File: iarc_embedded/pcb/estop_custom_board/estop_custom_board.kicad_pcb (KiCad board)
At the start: 2 copper layers, 5 parts, among them J1 RECEIVER, Q1 IRF8301M, Q2 IRF8301M, Q3 IRF8301M, U1 LM341T-05_TO220

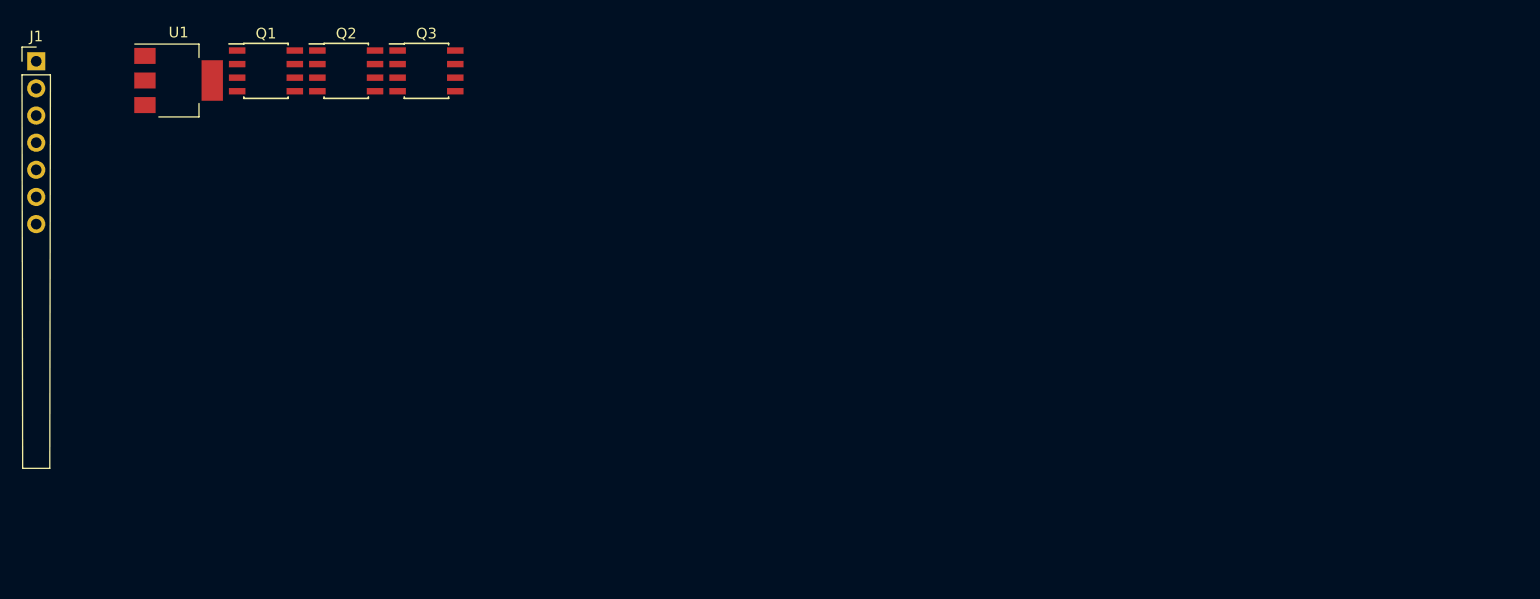
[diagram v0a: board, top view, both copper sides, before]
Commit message: NodeMCU ESP8266 embedded
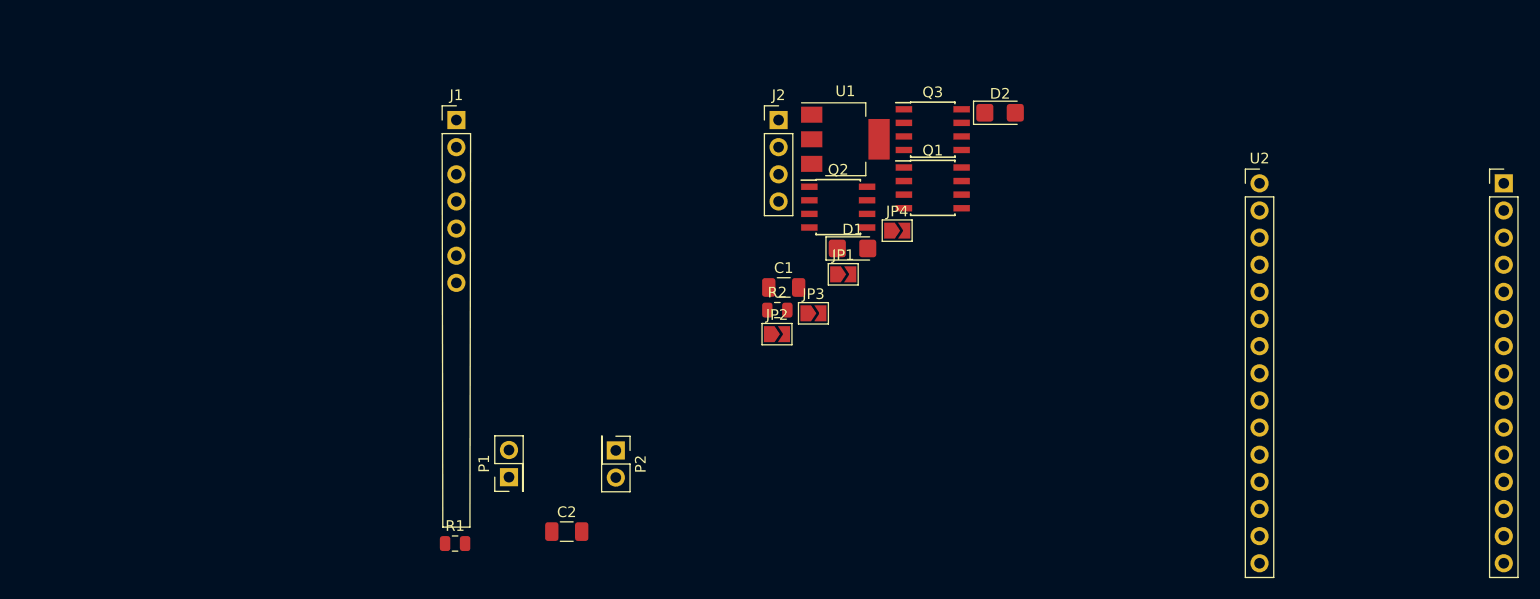
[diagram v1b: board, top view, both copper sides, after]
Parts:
- added C1: 4.7uF, Capacitor_SMD:C_1206_3216Metric, F.Cu at (198.7, 103.2)
- added C2: 10uF, Capacitor_SMD:C_1206_3216Metric, F.Cu at (178.4, 126.1)
- added D1: LED_GREEN, LED_SMD:LED_1206_3216Metric_Castellated, F.Cu at (205.2, 99.6)
- added D2: LED_RED, LED_SMD:LED_1206_3216Metric_Castellated, F.Cu at (219.0, 86.9)
- added J2: Conn_01x04, Connector_PinHeader_2.54mm:PinHeader_1x04_P2.54mm_Vertical, F.Cu at (198.2, 87.6)
- added JP1: Jumper, Jumper:SolderJumper-2_P1.3mm_Open_TrianglePad1.0x1.5mm, F.Cu at (204.3, 102.0)
- added JP2: Jumper, Jumper:SolderJumper-2_P1.3mm_Open_TrianglePad1.0x1.5mm, F.Cu at (198.1, 107.6)
- added JP3: Jumper, Jumper:SolderJumper-2_P1.3mm_Open_TrianglePad1.0x1.5mm, F.Cu at (201.5, 105.7)
- added JP4: Jumper, Jumper:SolderJumper-2_P1.3mm_Open_TrianglePad1.0x1.5mm, F.Cu at (209.3, 97.9)
- added P1: HEADER2, Connector_PinHeader_2.54mm:PinHeader_2x01_P2.54mm_Vertical, F.Cu at (173.0, 121.0)
- added P2: TOMOTORS, Connector_PinHeader_2.54mm:PinHeader_2x01_P2.54mm_Vertical, F.Cu at (183.0, 118.5)
- added R1: 475, Resistor_SMD:R_0805_2012Metric, F.Cu at (168.0, 127.2)
- added R2: 475, Resistor_SMD:R_0805_2012Metric, F.Cu at (198.1, 105.4)
- added U2: ESP8266-nodemcu, roomba_pcb:NODEMCU, F.Cu at (243.2, 93.5)
- moved Q1 63.4 mm to (212.7, 93.9)
- moved U1 62.7 mm to (204.5, 89.4)
- moved Q2 47.8 mm to (203.8, 95.7)
- moved Q3 47.7 mm to (212.7, 88.5)
- moved J1 39.7 mm to (168.1, 87.6)
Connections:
- J1 pad 3: (no net) -> Net-(J1-Pad3)
- J1 pad 4: (no net) -> Net-(J1-Pad4)
- J1 pad 5: (no net) -> Net-(J1-Pad5)
- J1 pad 6: (no net) -> Net-(J1-Pad6)
- U1 pad 1: (no net) -> +BATT

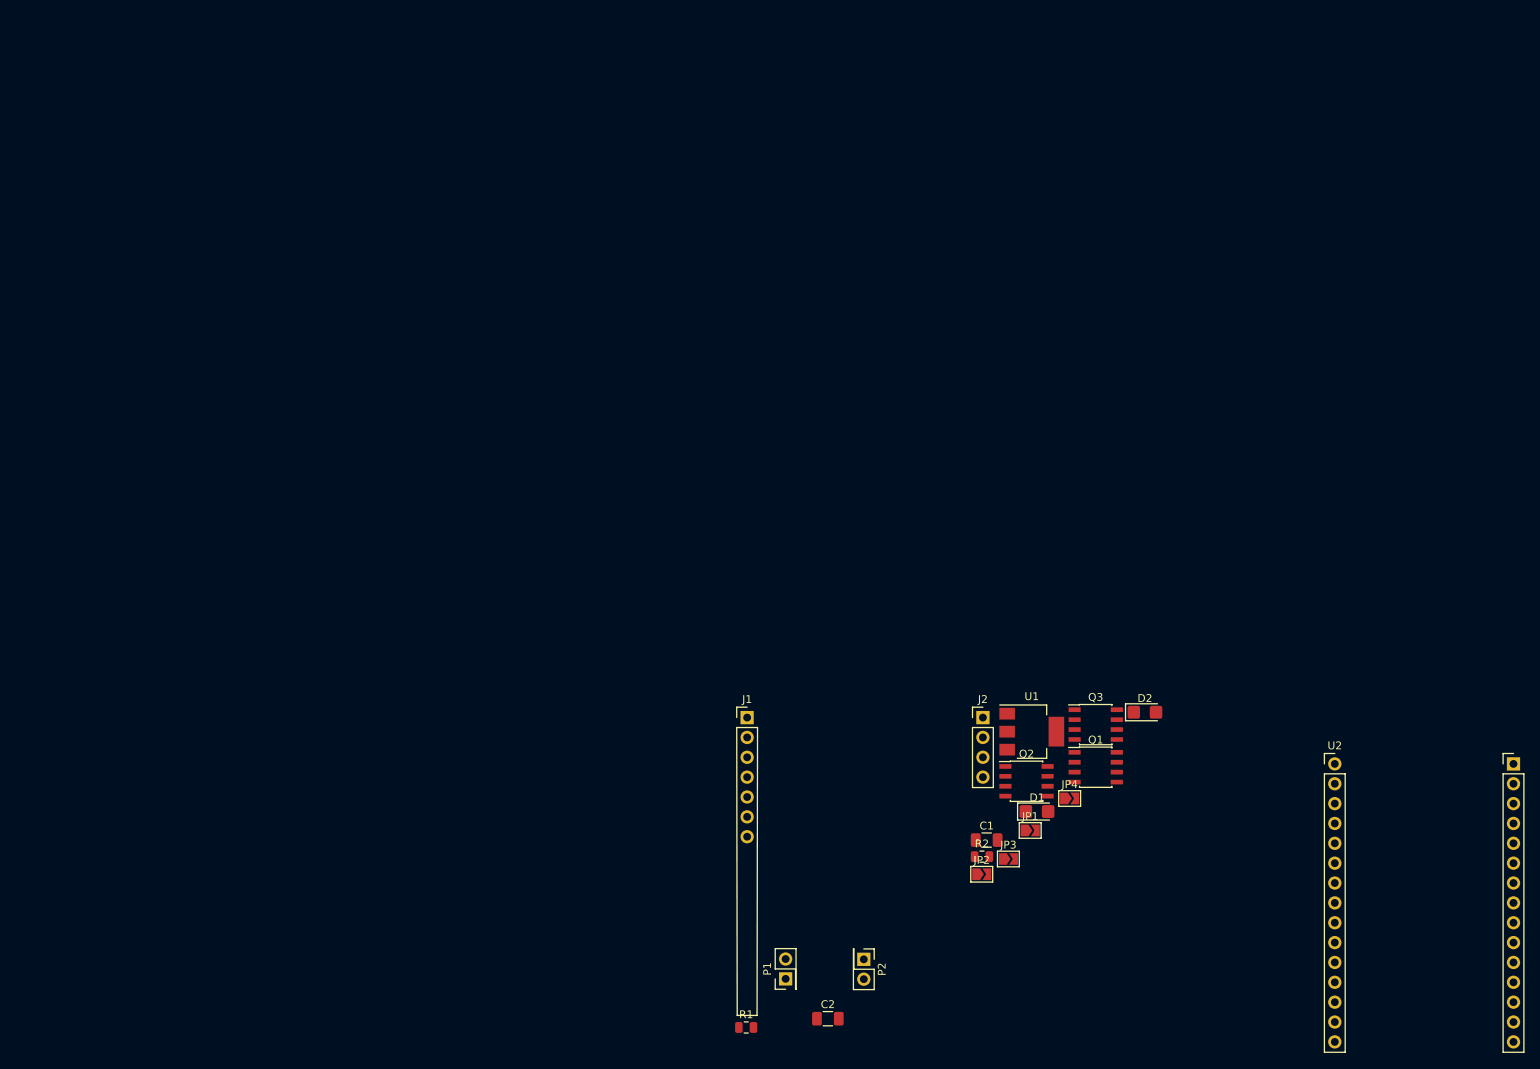
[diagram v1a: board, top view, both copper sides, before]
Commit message: PCB is laid out
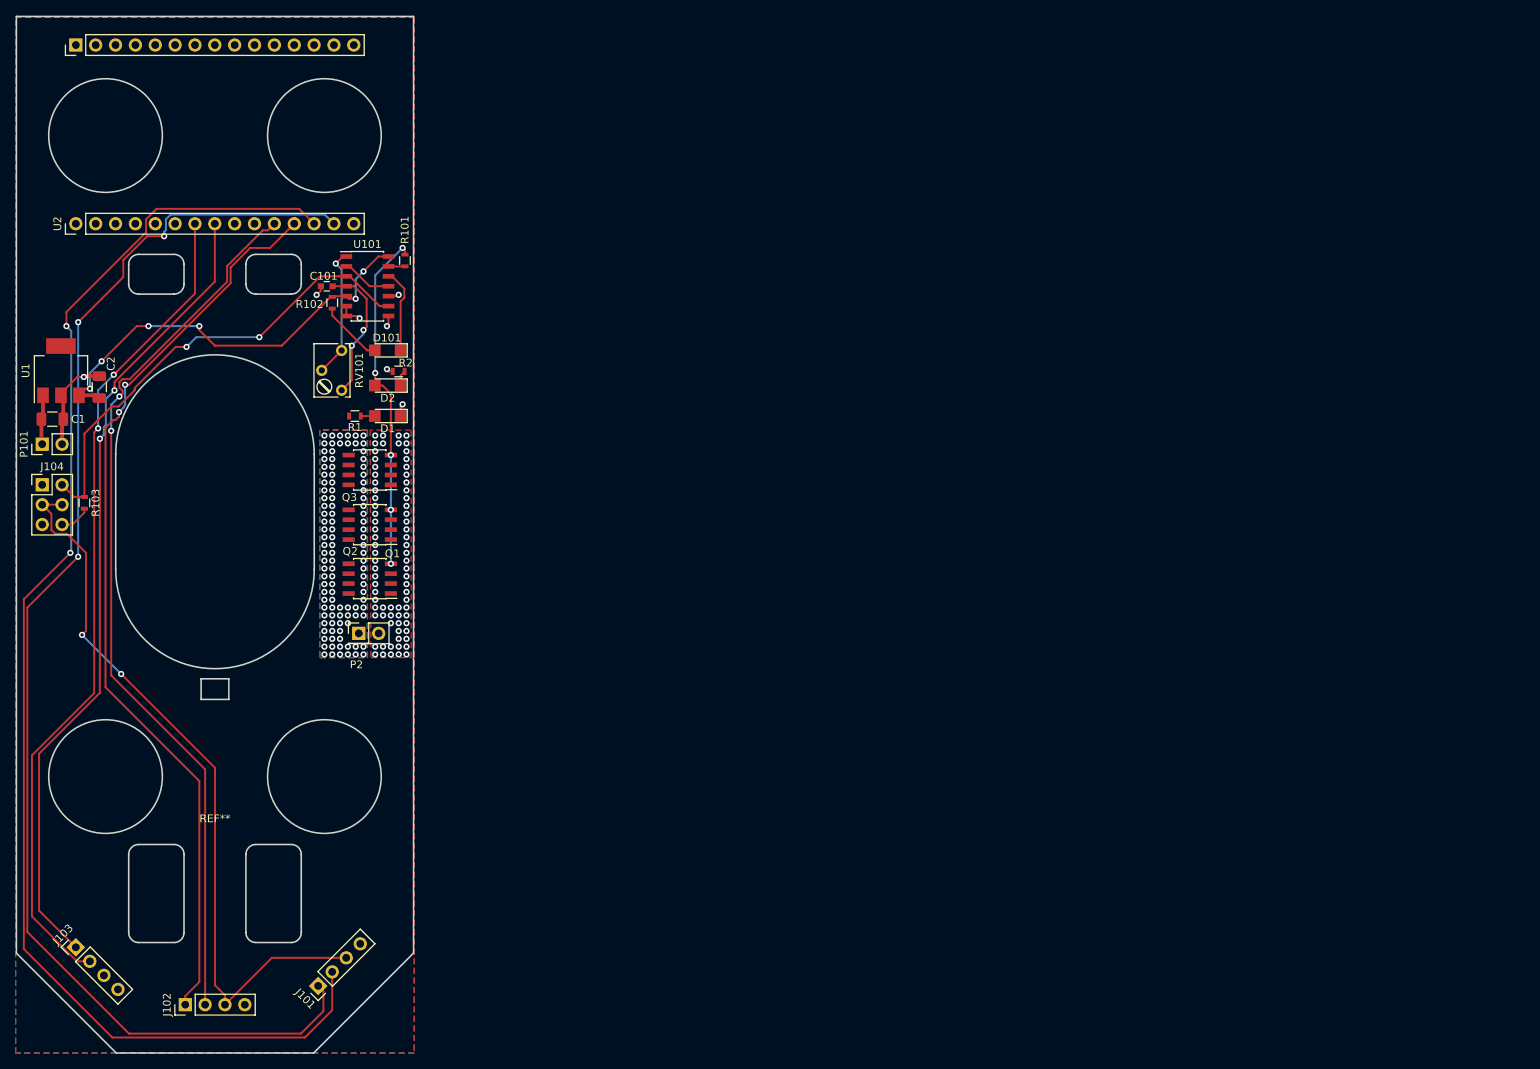
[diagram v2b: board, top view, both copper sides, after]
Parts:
- removed J1: RECEIVER, roomba_pcb:Receiver_IARC
- removed J2: Conn_01x04, Connector_PinHeader_2.54mm:PinHeader_1x04_P2.54mm_Vertical
- removed JP1, JP2, JP3, JP4: Jumper, Jumper:SolderJumper-2_P1.3mm_Open_TrianglePad1.0x1.5mm
- removed P1: HEADER2, Connector_PinHeader_2.54mm:PinHeader_2x01_P2.54mm_Vertical
- added C101: 1uF, Capacitors_SMD:C_0603, F.Cu at (114.3, 32.4)
- added D101: LED_RED, LEDs:LED_1206, F.Cu at (122.1, 40.6)
- added J101: Conn_01x04, Pin_Headers:Pin_Header_Straight_1x04_Pitch2.54mm, F.Cu at (113.2, 121.9)
- added J102: Conn_01x04, Pin_Headers:Pin_Header_Straight_1x04_Pitch2.54mm, F.Cu at (96.2, 124.3)
- added J103: Conn_01x04, Pin_Headers:Pin_Header_Straight_1x04_Pitch2.54mm, F.Cu at (82.2, 117.0)
- added J104: Conn_02x03_Odd_Even, Pin_Headers:Pin_Header_Straight_2x03_Pitch2.54mm, F.Cu at (77.9, 57.8)
- added P101: BATT, Pin_Headers:Pin_Header_Straight_1x02_Pitch2.54mm, F.Cu at (77.9, 52.6)
- added R101: 10, Resistors_SMD:R_0603, F.Cu at (124.3, 29.1)
- added R102: 475, Resistors_SMD:R_0603, F.Cu at (115.0, 34.5)
- added R103: 10k, Resistors_SMD:R_0603, F.Cu at (83.3, 60.1)
- added REF**: Outline, roomba_pcb:Outline, F.Cu at (100.0, 100.0)
- added RV101: 5k, Potentiometers:Potentiometer_Trimmer_Bourns_3266W, F.Cu at (116.2, 45.7)
- added U101: CD4013BM, Housings_SOIC:SOIC-14_3.9x8.7mm_Pitch1.27mm, F.Cu at (119.5, 32.4)
- D1, D2: footprint LED_SMD:LED_1206_3216Metric_Castellated -> LEDs:LED_1206
- P2: value TOMOTORS -> GND_INTERUPT
- R1, R2: footprint Resistor_SMD:R_0805_2012Metric -> Resistors_SMD:R_0603
- moved U2 175.2 mm to (82.2, 24.4), turned to 90 degrees
- moved U1 132.5 mm to (80.3, 43.2), turned to 90 degrees
- moved C1 131.1 mm to (79.2, 49.4)
- moved C2 123.3 mm to (85.2, 45.3), turned to 90 degrees
- moved D2 105.5 mm to (122.1, 45.1), turned to 180 degrees
- moved Q3 98.4 mm to (119.8, 55.9), turned to 180 degrees
- moved D1 97.3 mm to (122.1, 49.0), turned to 180 degrees
- moved R2 97.1 mm to (123.5, 43.3), turned to 180 degrees
- moved Q1 95.9 mm to (119.8, 69.8), turned to 180 degrees
- moved R1 92.9 mm to (117.9, 49.0), turned to 180 degrees
- moved Q2 90.2 mm to (119.8, 62.9), turned to 180 degrees
- moved P2 76.9 mm to (118.4, 76.8), turned to 0 degrees
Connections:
- P2 pad 1: +BATT -> Net-(P2-Pad1)
- P2 pad 2: Net-(P2-Pad2) -> GND
- Q1 pad 5: Net-(P2-Pad2) -> Net-(P2-Pad1)
- Q1 pad 6: Net-(P2-Pad2) -> Net-(P2-Pad1)
- Q1 pad 7: Net-(P2-Pad2) -> Net-(P2-Pad1)
- Q1 pad 8: Net-(P2-Pad2) -> Net-(P2-Pad1)
- Q2 pad 5: Net-(P2-Pad2) -> Net-(P2-Pad1)
- Q2 pad 6: Net-(P2-Pad2) -> Net-(P2-Pad1)
- Q2 pad 7: Net-(P2-Pad2) -> Net-(P2-Pad1)
- Q2 pad 8: Net-(P2-Pad2) -> Net-(P2-Pad1)
- Q3 pad 5: Net-(P2-Pad2) -> Net-(P2-Pad1)
- Q3 pad 6: Net-(P2-Pad2) -> Net-(P2-Pad1)
- Q3 pad 7: Net-(P2-Pad2) -> Net-(P2-Pad1)
- Q3 pad 8: Net-(P2-Pad2) -> Net-(P2-Pad1)
- U2 pad 22: (no net) -> /R_RX
- U2 pad 23: (no net) -> /R_PW
- U2 pad 26: (no net) -> /C_RX
- U2 pad 27: (no net) -> /C_PW
- U2 pad 28: (no net) -> /L_RX
- U2 pad 29: (no net) -> /L_PW
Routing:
- net /L_RX: track 0.00 -> 173.7 mm, vias 0 -> 2
- net /L_PW: track 0.00 -> 170.0 mm, vias 0 -> 3
- net +5V: track 0.00 -> 150.4 mm, vias 0 -> 8
- net /C_PW: track 0.00 -> 117.5 mm, vias 0 -> 2
- net /C_RX: track 0.00 -> 114.8 mm, vias 0 -> 2
- net /R_RX: track 0.00 -> 107.0 mm, vias 0 -> 2
- net /R_PW: track 0.00 -> 103.8 mm, vias 0 -> 2
- net /S_IN: track 0.00 -> 60.6 mm, vias 0 -> 2
- net /GATE: track 0.00 -> 44.3 mm, vias 0 -> 5
- net GND: track 0.00 -> 26.1 mm, vias 0 -> 82
- net Net-(C101-Pad1): track 0.00 -> 18.0 mm, vias 0 -> 2
- net Net-(RV101-Pad2): track 0.00 -> 16.7 mm, vias 0 -> 1
- net Net-(D101-Pad1): track 0.00 -> 10.8 mm
- net Net-(D101-Pad2): track 0.00 -> 8.19 mm
- net Net-(U101-Pad11): track 0.00 -> 6.45 mm
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- added copper zone on F.Cu, net +5V
- added copper zone on B.Cu, net GND
- added copper zone on F.Cu, net GND
- added copper zone on B.Cu, net Net-(P2-Pad1)
- added copper zone on F.Cu, net Net-(P2-Pad1)
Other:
- board outline added: 50.8 x 132.6 mm
